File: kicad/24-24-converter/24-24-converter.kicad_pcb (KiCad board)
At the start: 4 copper layers, 143.5 x 76 mm, 78 parts, among them J1 Conn_01x02, J2 Conn_01x02, M1 CSD18540Q5B, M1_1 CSD18540Q5B, M2 CSD18540Q5B, M2_1 CSD18540Q5B, M3 GENERIC_MOSFET_N, M3_1 GENERIC_MOSFET_N, M4 GENERIC_MOSFET_N, U1 LM5176PWPR

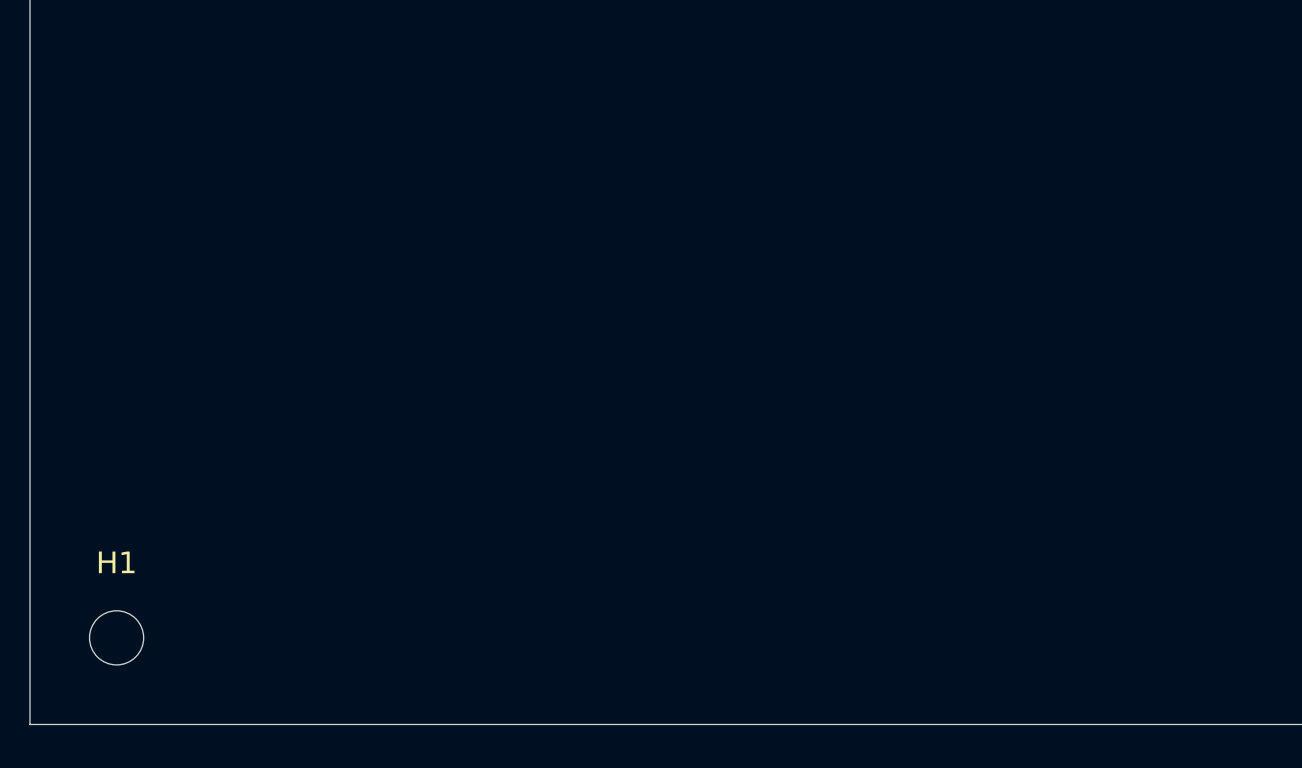
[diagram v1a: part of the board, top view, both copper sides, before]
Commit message: added logo to pcb
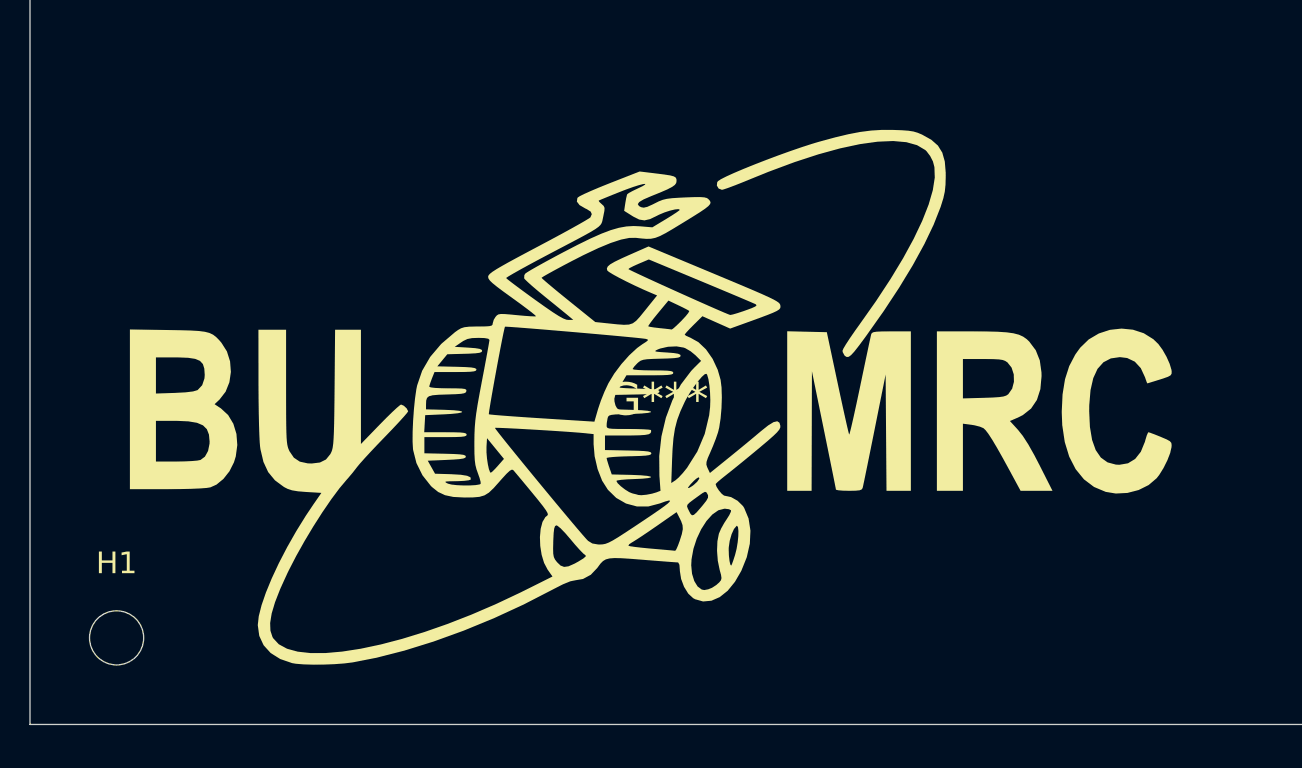
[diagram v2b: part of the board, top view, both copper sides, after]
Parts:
- added G***: LOGO, LOGO, F.Cu at (98.0, 114.0)

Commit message: added documents
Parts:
- moved R2 0.45 mm to (183.0, 56.5), turned to 0 degrees
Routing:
- net VOUT: track 230.0 -> 222.4 mm
- net Net-(D3-A): track 7.76 -> 2.98 mm
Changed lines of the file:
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@@
 	(footprint "Resistor_SMD:R_1206_3216Metric_Pad1.30x1.75mm_HandSolder"
 		(layer "F.Cu")
-		(at 182.55 56.515 180)
+		(at 183 56.5)
 		(descr "Resistor SMD 1206 (3216 Metric), square (rectangular) end terminal, IPC-7351 nominal with elongated pad for handsoldering. (Body size source: IPC-SM-782 page 72, https://www.pcb-3d.com/wordpress/wp-content/uploads/ipc-sm-782a_amendment_1_and_2.pdf)")
 		(tags "resistor handsolder")
@@
 		(duplicate_pad_numbers_are_jumpers no)
 		(fp_line
-			(start -0.727064 0.91)
-			(end 0.727064 0.91)
+			(start -0.727064 -0.91)
+			(end 0.727064 -0.91)
 			(stroke
 				(width 0.12)
@@
 		)
 		(fp_line
-			(start -0.727064 -0.91)
-			(end 0.727064 -0.91)
+			(start -0.727064 0.91)
+			(end 0.727064 0.91)
 			(stroke
 				(width 0.12)
@@
 		)
 		(pad "1" smd roundrect
-			(at -1.55 0 180)
+			(at -1.55 0)
 			(size 1.3 1.75)
 			(layers "F.Cu" "F.Mask" "F.Paste")
@@
 		)
 		(pad "2" smd roundrect
-			(at 1.55 0 180)
+			(at 1.55 0)
 			(size 1.3 1.75)
 			(layers "F.Cu" "F.Mask" "F.Paste")
@@
 	)
 	(segment
+		(start 181.45 58.774744)
+		(end 181.45 56.5)
+		(width 0.2)
+		(layer "F.Cu")
+		(net "VOUT")
+	)
+	(segment
 		(start 169.545 82.7825)
 		(end 169.545 80.636)
@@
 	)
 	(segment
-		(start 182.585 55)
-		(end 179.5 55)
-		(width 0.2)
-		(layer "F.Cu")
-		(net "VOUT")
-	)
-	(segment
 		(start 172.085 87.2275)
 		(end 175 87.2275)
@@
 	)
 	(segment
-		(start 179.5 56.824744)
-		(end 194.640256 71.965)
-		(width 0.2)
-		(layer "F.Cu")
-		(net "VOUT")
-	)
-	(segment
 		(start 161.925 82.7825)
 		(end 159.385 82.7825)
@@
 	)
 	(segment
-		(start 184.1 56.515)
-		(end 182.585 55)
-		(width 0.2)
-		(layer "F.Cu")
-		(net "VOUT")
-	)
-	(segment
 		(start 161.925 82.7825)
 		(end 161.925 80.636)
@@
 	)
 	(segment
-		(start 179.5 55)
-		(end 179.5 56.824744)
-		(width 0.2)
-		(layer "F.Cu")
-		(net "VOUT")
-	)
-	(segment
 		(start 152.5 87)
 		(end 151.5 87)
@@
 	)
 	(segment
+		(start 194.640256 71.965)
+		(end 181.45 58.774744)
+		(width 0.2)
+		(layer "F.Cu")
+		(net "VOUT")
+	)
+	(segment
 		(start 175 87.2275)
 		(end 176.7725 87.2275)
@@
 	)
 	(segment
-		(start 186.04 58)
-		(end 187.525 56.515)
-		(width 0.2)
-		(layer "F.Cu")
-		(net "Net-(D3-A)")
-	)
-	(segment
-		(start 181 56.515)
-		(end 182.485 58)
+		(start 187.525 56.515)
+		(end 184.565 56.515)
 		(width 0.2)
 		(layer "F.Cu")
@@
 	)
 	(segment
-		(start 182.485 58)
-		(end 186.04 58)
+		(start 184.565 56.515)
+		(end 184.55 56.5)
 		(width 0.2)
 		(layer "F.Cu")

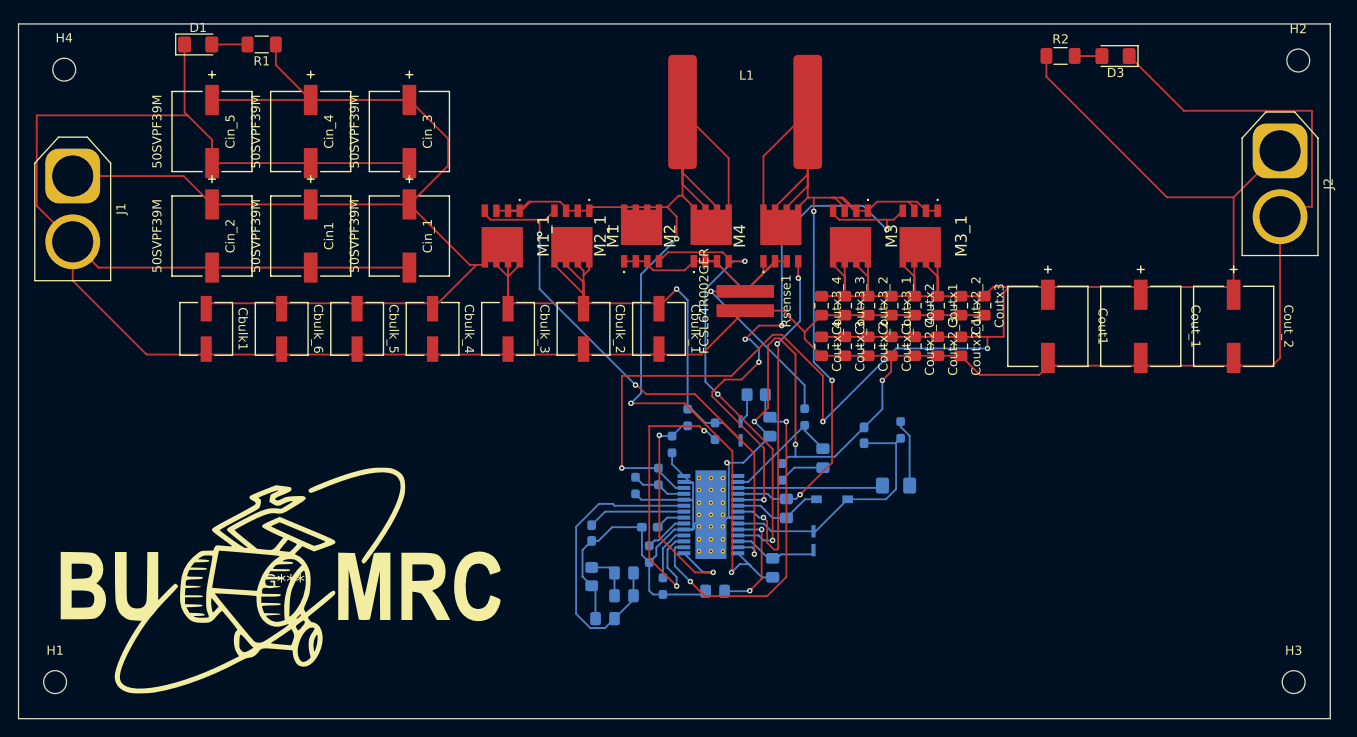
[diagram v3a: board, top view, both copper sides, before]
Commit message: added filled zones
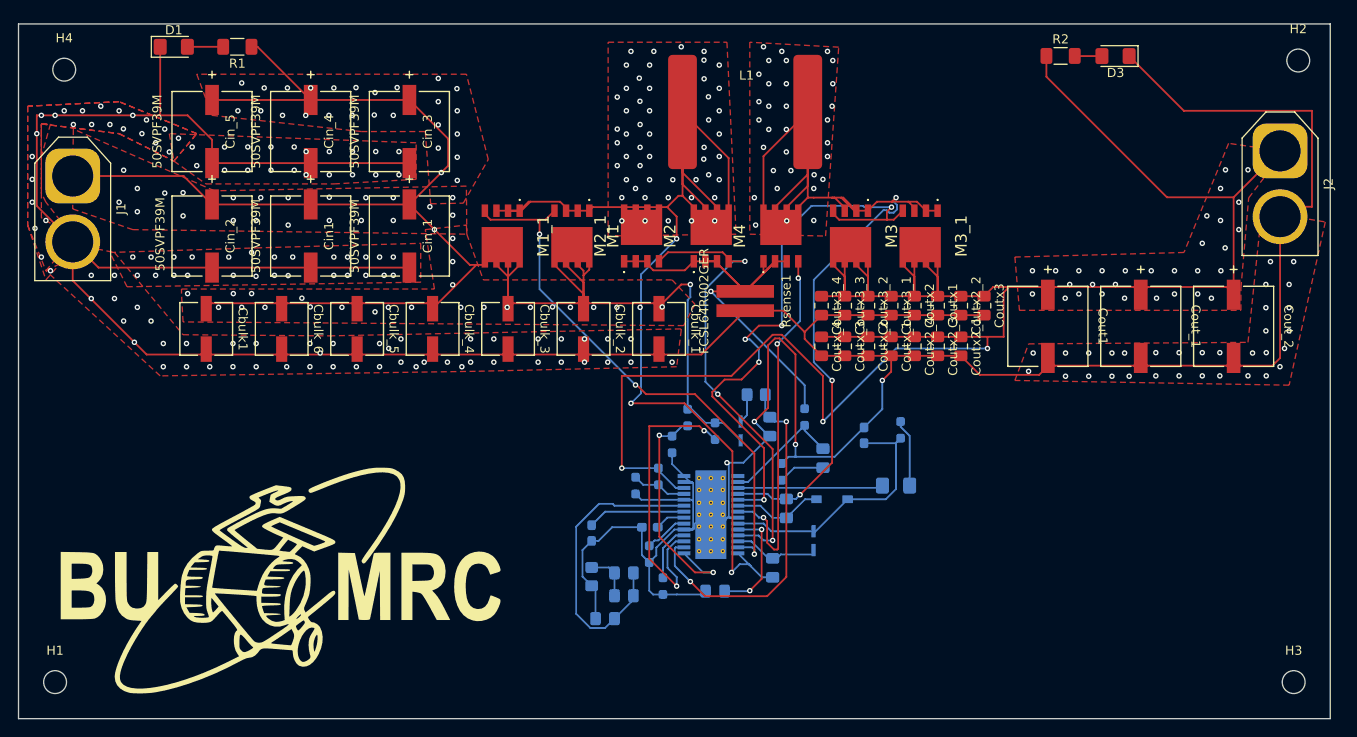
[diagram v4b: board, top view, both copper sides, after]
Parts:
- moved D1 2.68 mm to (86.0, 55.5)
- moved R1 2.68 mm to (92.9, 55.5)
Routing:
- net /SW2: track 109.8 -> 115.7 mm, vias 3 -> 35
- net VIN: track 197.7 -> 200.7 mm, vias 1 -> 75
- net GND: track 450.2 -> 449.7 mm, vias 4 -> 155
- net VOUT: vias 3 -> 33
- net /SW1: vias 3 -> 54
- added copper zone on F.Cu, net /SW1
- added copper zone on In1.Cu, net /SW1
- added copper zone on F.Cu, net /SW2
- added copper zone on In1.Cu, net /SW2
- added copper zone on F.Cu, net GND
- added copper zone on In1.Cu, net GND
- added copper zone on F.Cu, net VIN
- added copper zone on In1.Cu, net VIN
- added copper zone on F.Cu, net VOUT
- added copper zone on In1.Cu, net VOUT

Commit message: moved via's
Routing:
- net VIN: vias 75 -> 77
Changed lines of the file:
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@@
 	)
 	(via
-		(at 139.42 83.96)
+		(at 139 82)
 		(size 0.6)
 		(drill 0.3)
@@
 	)
 	(via
-		(at 90.88 84)
+		(at 91 83)
 		(size 0.6)
 		(drill 0.3)
@@
 	)
 	(via
-		(at 100.96 60)
+		(at 102 59)
 		(size 0.6)
 		(drill 0.3)
@@
 	)
 	(via
-		(at 104.38 84)
+		(at 84 70.5)
 		(size 0.6)
 		(drill 0.3)
@@
 	)
 	(via
-		(at 93.42 59.46)
+		(at 103 82.5)
 		(size 0.6)
 		(drill 0.3)
@@
 	)
 	(via
-		(at 134.46 84)
+		(at 93 59.5)
+		(size 0.6)
+		(drill 0.3)
+		(layers "F.Cu" "B.Cu")
+		(free yes)
+		(net "VIN")
+	)
+	(via
+		(at 135 84.5)
 		(size 0.6)
 		(drill 0.3)
@@
 	)
 	(via
-		(at 137 84)
+		(at 78.5 67.5)
+		(size 0.6)
+		(drill 0.3)
+		(layers "F.Cu" "B.Cu")
+		(free yes)
+		(net "VIN")
+	)
+	(via
+		(at 136.5 82.5)
 		(size 0.6)
 		(drill 0.3)
@@
 	)
 	(via
-		(at 129.38 84)
+		(at 129 82.5)
 		(size 0.6)
 		(drill 0.3)
@@
 	)
 	(via
-		(at 100.42 63)
+		(at 100.5 63.5)
 		(size 0.6)
 		(drill 0.3)
@@
 	)
 	(via
-		(at 117.38 84)
+		(at 118.5 84)
 		(size 0.6)
 		(drill 0.3)
@@
 	)
 	(via
-		(at 112 84)
+		(at 111.5 82.5)
 		(size 0.6)
 		(drill 0.3)
@@
 	)
 	(via
-		(at 110.42 59.96)
+		(at 110 59.5)
 		(size 0.6)
 		(drill 0.3)
@@
 	)
 	(via
-		(at 95.96 84)
+		(at 96 83)
 		(size 0.6)
 		(drill 0.3)
@@
 	)
 	(via
-		(at 119.92 84)
+		(at 118.5 82)
 		(size 0.6)
 		(drill 0.3)
@@
 	)
 	(via
-		(at 127.42 83.96)
+		(at 127 84.5)
 		(size 0.6)
 		(drill 0.3)
@@
 	)
 	(via
-		(at 100.92 83.96)
+		(at 102 84.5)
 		(size 0.6)
 		(drill 0.3)
@@
 	)
 	(via
-		(at 109.46 84)
+		(at 110 84.5)
 		(size 0.6)
 		(drill 0.3)
@@
 	)
 	(via
-		(at 125 84)
+		(at 125.4 82)
 		(size 0.6)
 		(drill 0.3)
@@
 	)
 	(via
-		(at 108 84.5)
+		(at 108 82.5)
 		(size 0.6)
 		(drill 0.3)
@@
 	)
 	(via
-		(at 131.92 84)
+		(at 133 82)
 		(size 0.6)
 		(drill 0.3)
@@
 	)
 	(via
-		(at 87.5 82.5)
+		(at 87.5 83)
 		(size 0.6)
 		(drill 0.3)
@@
 	)
 	(via
-		(at 122.46 84)
+		(at 120.5 82.5)
 		(size 0.6)
 		(drill 0.3)
@@
 	)
 	(via
-		(at 95 87.96)
+		(at 94 87.96)
 		(size 0.6)
 		(drill 0.3)
@@
 	)
 	(via
-		(at 108.5 87.96)
+		(at 109.5 87.5)
 		(size 0.6)
 		(drill 0.3)
@@
 	)
 	(via
-		(at 130.92 87.46)
+		(at 135 89.1651)
 		(size 0.6)
 		(drill 0.3)
@@
 	)
 	(via
-		(at 121 90)
+		(at 120 90.5)
 		(size 0.6)
 		(drill 0.3)
@@
 	)
 	(via
-		(at 87.38 87.96)
+		(at 85.5 86.5)
 		(size 0.6)
 		(drill 0.3)
@@
 	)
 	(via
-		(at 109.5 88.5)
+		(at 109.5 89.1651)
 		(size 0.6)
 		(drill 0.3)
@@
 	)
 	(via
-		(at 128.38 87.46)
+		(at 127.5 88)
 		(size 0.6)
 		(drill 0.3)
@@
 	)
 	(via
-		(at 103.42 87.96)
+		(at 102.5 88)
 		(size 0.6)
 		(drill 0.3)
@@
 	)
 	(via
-		(at 100.88 87.96)
+		(at 101.5 87.96)
 		(size 0.6)
 		(drill 0.3)
@@
 	)
 	(via
-		(at 92.46 87.96)
+		(at 93 87.96)
 		(size 0.6)
 		(drill 0.3)
@@
 	)
 	(via
-		(at 133.46 87.46)
+		(at 134.5 87.5)
 		(size 0.6)
 		(drill 0.3)
@@
 	)
 	(via
-		(at 118.46 90)
+		(at 124 90.5)
 		(size 0.6)
 		(drill 0.3)
@@
 	)
 	(via
-		(at 121 87.46)
+		(at 118.5 89.1651)
 		(size 0.6)
 		(drill 0.3)
@@
 	)
 	(via
-		(at 149.639998 75)
+		(at 149.5 69.5)
 		(size 0.6)
 		(drill 0.3)
@@
 	)
 	(via
-		(at 153.04 74.54)
+		(at 156.5 73.5)
 		(size 0.6)
 		(drill 0.3)
@@
 		(polygon
 			(pts
-				(xy 117.659941 72.602887) (xy 120.39071 67.824042) (xy 118 58.5) (xy 88.5 58.5) (xy 90.17 63) (xy 106.5 64.77)
+				(xy 117.659941 72.602887) (xy 120.39071 67.824042) (xy 118 58.5) (xy 88.5 58.5) (xy 88.5 63) (xy 106.5 64.77)
 				(xy 113.5 64.77) (xy 114.087413 72.676574)
 			)
@@
 		(polygon
 			(pts
-				(xy 149 55) (xy 159 55.5) (xy 157.5 76.5) (xy 149 76)
+				(xy 149 55) (xy 158.75089 55.487544) (xy 157.251046 76.485356) (xy 149 76)
 			)
 		)
@@
 		(polygon
 			(pts
-				(xy 114 72.5) (xy 118 72.5) (xy 120.5 67.5) (xy 118 58) (xy 88 58.5) (xy 90 63) (xy 105.5 65) (xy 113.5 65)
+				(xy 114 72.5) (xy 118 72.5) (xy 120.5 67.5) (xy 118 58) (xy 88 58.5) (xy 88.5 63) (xy 105.5 65)
+				(xy 113.5 65)
 			)
 		)

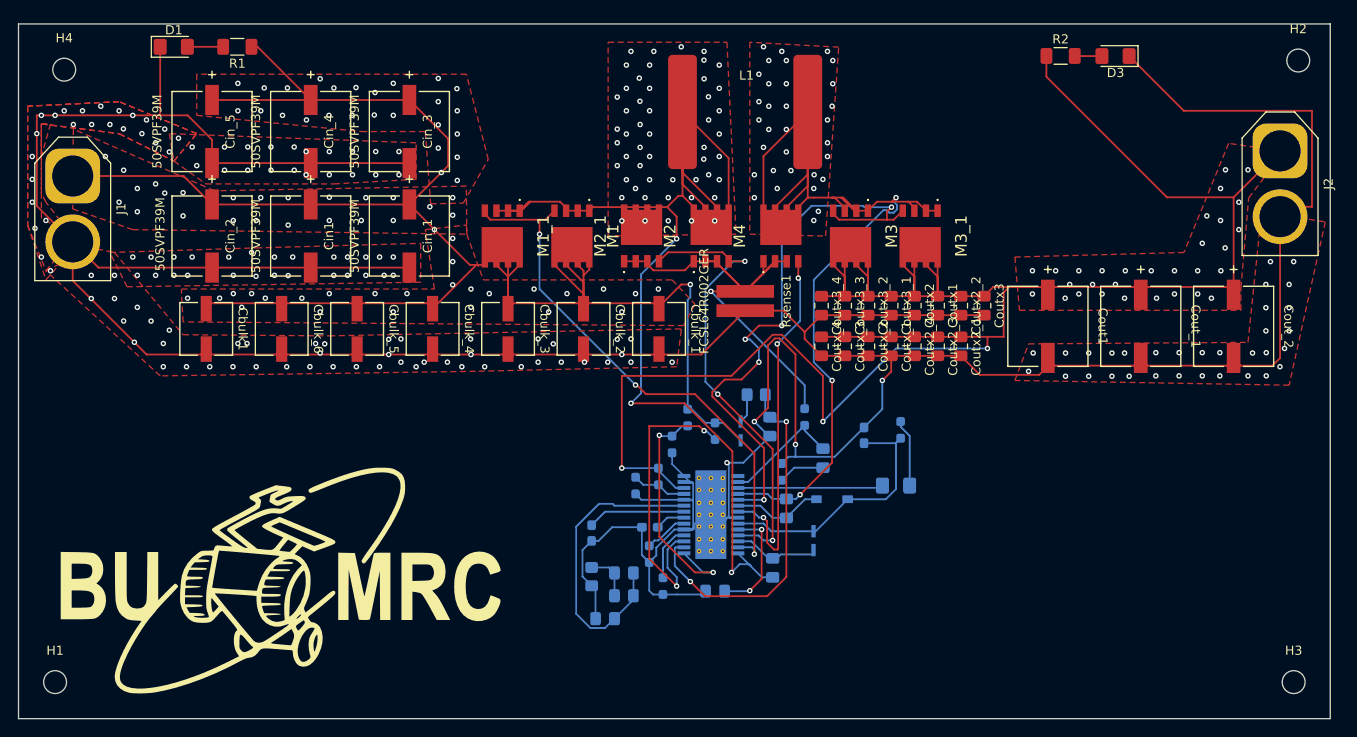
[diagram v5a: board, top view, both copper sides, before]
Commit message: added high current paths to Coutx
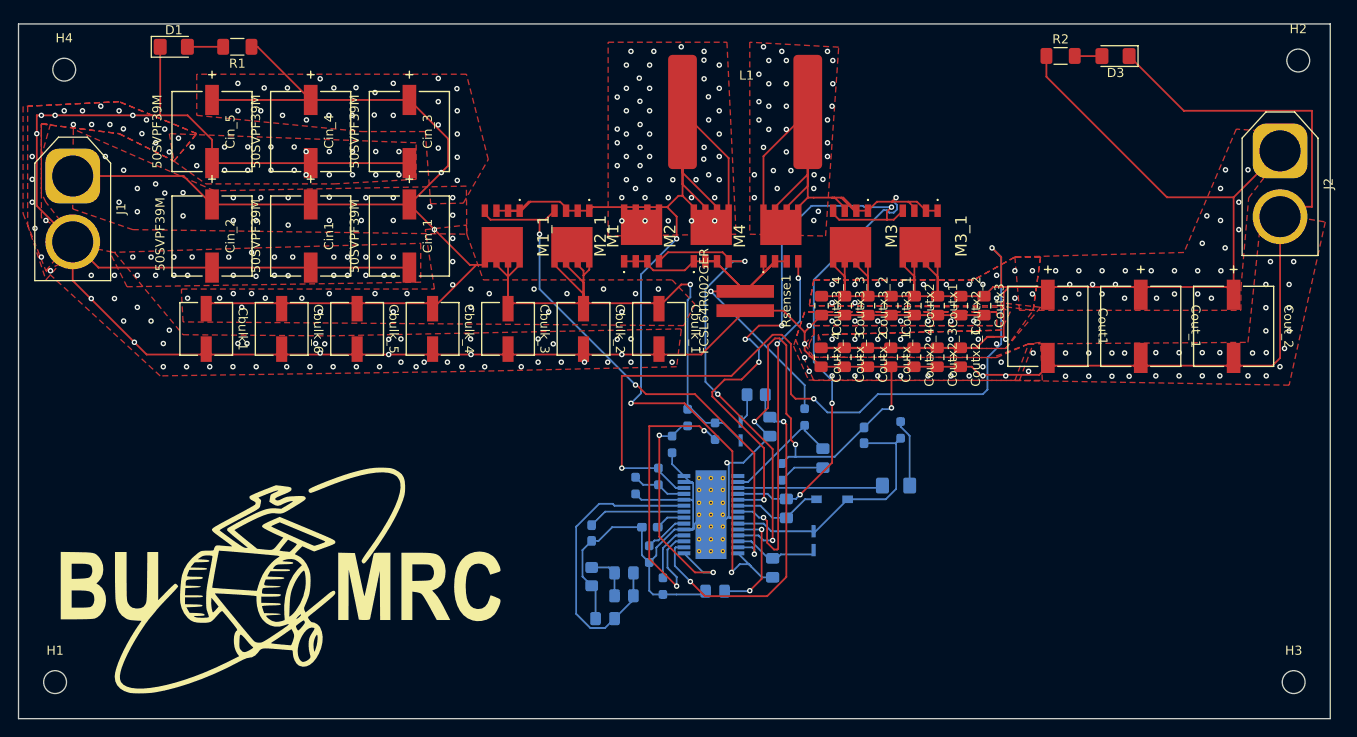
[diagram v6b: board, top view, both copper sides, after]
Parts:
- moved Coutx2_1 1.20 mm to (172.0, 89.5)
- moved Coutx_1 1.20 mm to (164.4, 89.5)
- moved Coutx_2 1.20 mm to (161.9, 89.5)
- moved Coutx2_3 1.20 mm to (169.5, 89.5)
- moved Coutx2_4 1.20 mm to (167.0, 89.5)
- moved Coutx_3 1.20 mm to (159.3, 89.5)
- moved Coutx_4 1.20 mm to (156.8, 89.5)
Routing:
- net VOUT: track 222.4 -> 241.3 mm, vias 33 -> 56
- net GND: track 449.7 -> 449.2 mm, vias 155 -> 177
- added copper zone on F.Cu, net (none)
